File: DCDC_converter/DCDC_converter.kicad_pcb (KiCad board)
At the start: 2 copper layers, 65 x 27 mm, 27 parts, among them J1 Conn_01x02, J2 Conn_01x02, U1 MP2491C

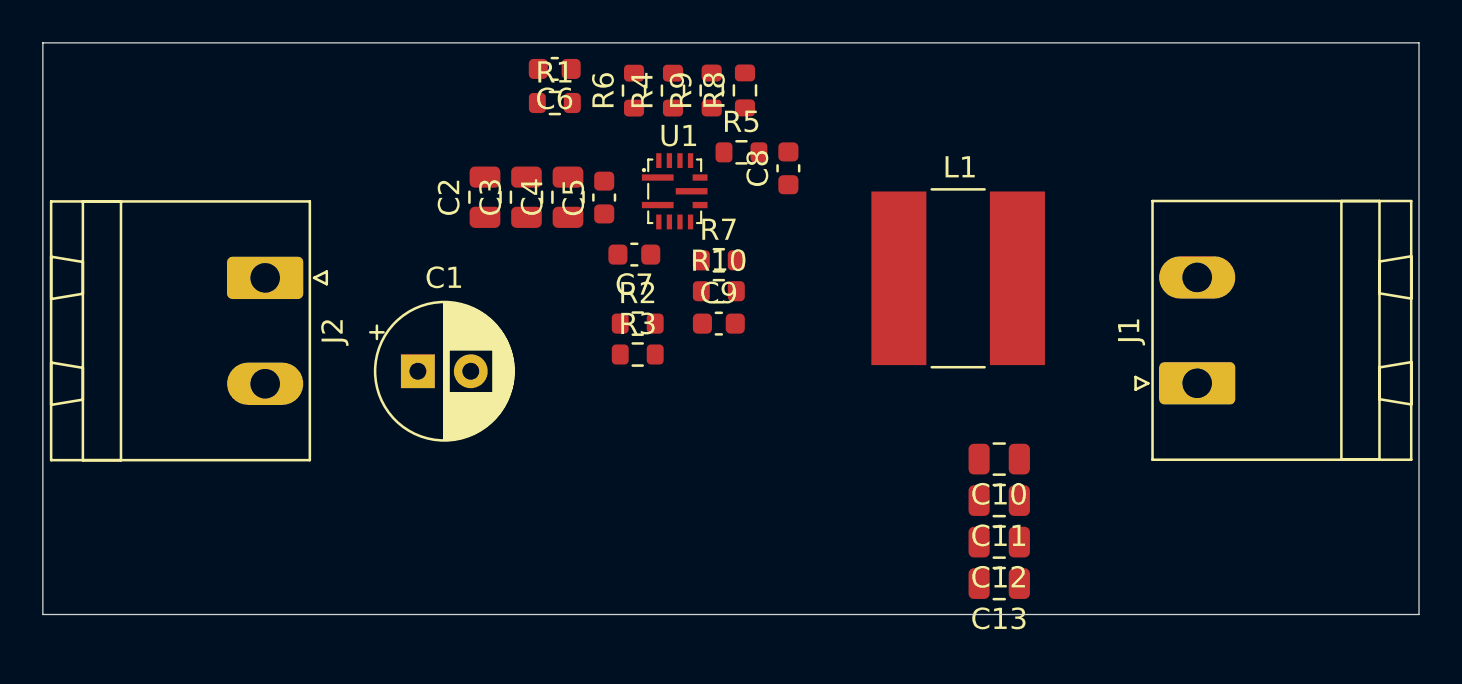
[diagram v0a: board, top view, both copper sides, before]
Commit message: Adjusting elements placement
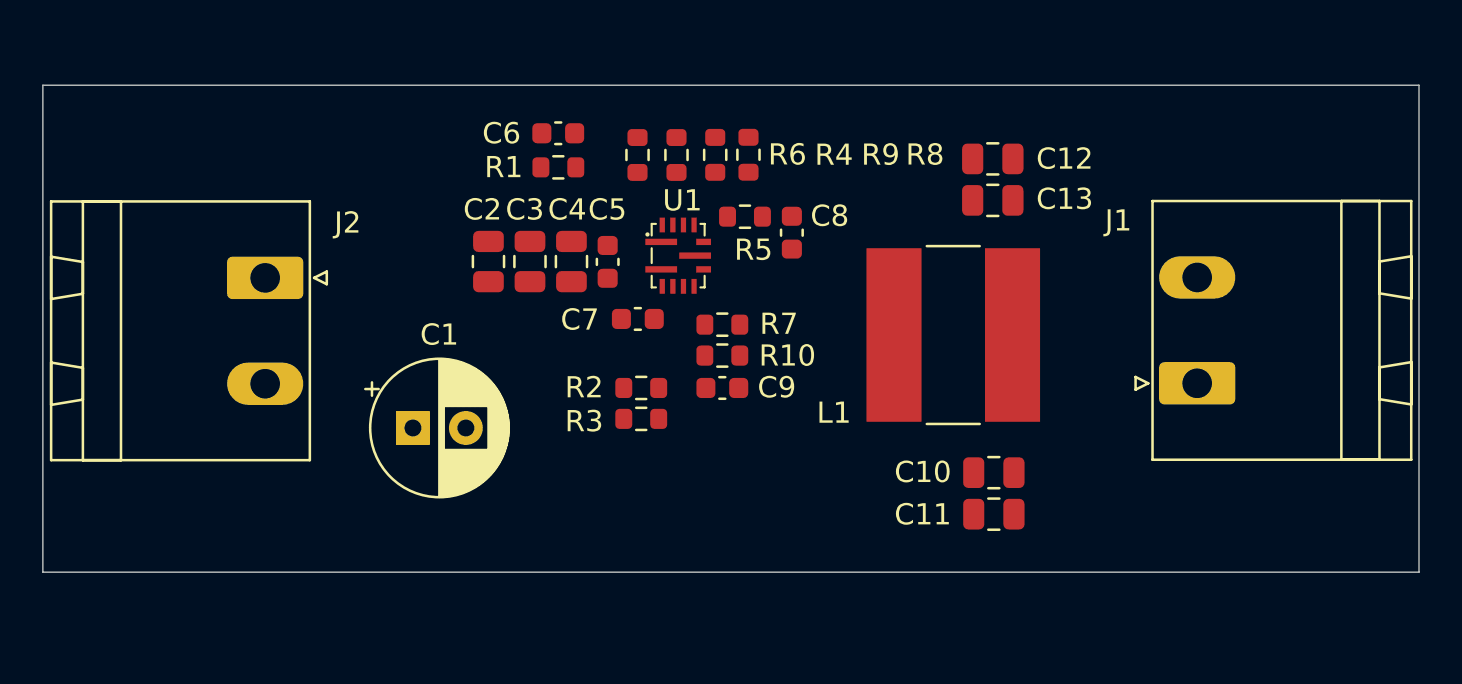
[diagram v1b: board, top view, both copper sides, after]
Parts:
- moved C12 18.1 mm to (204.4, 84.2)
- moved C13 18.1 mm to (204.4, 86.1)
- moved C5 3.04 mm to (186.2, 89.0)
- moved R4 3.04 mm to (189.4, 84.0)
- moved C4 3.04 mm to (184.5, 89.0)
- moved C8 3.04 mm to (194.9, 87.7)
- moved C9 3.04 mm to (191.6, 95.0)
- moved R2 3.04 mm to (187.8, 95.0)
- moved R6 3.04 mm to (187.6, 84.0)
- moved R7 3.04 mm to (191.6, 92.0)
- moved R8 3.04 mm to (192.8, 84.0)
- moved U1 3.04 mm to (189.5, 88.8)
- moved C2 3.04 mm to (180.5, 89.0)
- moved C3 3.04 mm to (182.5, 89.0)
- moved C6 3.04 mm to (183.8, 83.0)
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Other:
- board size 65 x 27 mm -> 65 x 23 mm

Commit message: Changing number of layers of PCB
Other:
- copper layers 2 -> 4
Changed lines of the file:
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@@
 	(layers
 		(0 "F.Cu" signal)
+		(1 "In1.Cu" signal)
+		(2 "In2.Cu" signal)
 		(31 "B.Cu" signal)
 		(32 "B.Adhes" user "B.Adhesive")
@@
 	)
 	(setup
+		(stackup
+			(layer "F.SilkS"
+				(type "Top Silk Screen")
+			)
+			(layer "F.Paste"
+				(type "Top Solder Paste")
+			)
+			(layer "F.Mask"
+				(type "Top Solder Mask")
+				(thickness 0.01)
+			)
+			(layer "F.Cu"
+				(type "copper")
+				(thickness 0.035)
+			)
+			(layer "dielectric 1"
+				(type "prepreg")
+				(thickness 0.1)
+				(material "FR4")
+				(epsilon_r 4.5)
+				(loss_tangent 0.02)
+			)
+			(layer "In1.Cu"
+				(type "copper")
+				(thickness 0.035)
+			)
+			(layer "dielectric 2"
+				(type "core")
+				(thickness 1.24)
+				(material "FR4")
+				(epsilon_r 4.5)
+				(loss_tangent 0.02)
+			)
+			(layer "In2.Cu"
+				(type "copper")
+				(thickness 0.035)
+			)
+			(layer "dielectric 3"
+				(type "prepreg")
+				(thickness 0.1)
+				(material "FR4")
+				(epsilon_r 4.5)
+				(loss_tangent 0.02)
+			)
+			(layer "B.Cu"
+				(type "copper")
+				(thickness 0.035)
+			)
+			(layer "B.Mask"
+				(type "Bottom Solder Mask")
+				(thickness 0.01)
+			)
+			(layer "B.Paste"
+				(type "Bottom Solder Paste")
+			)
+			(layer "B.SilkS"
+				(type "Bottom Silk Screen")
+			)
+			(copper_finish "None")
+			(dielectric_constraints no)
+		)
 		(pad_to_mask_clearance 0)
 		(allow_soldermask_bridges_in_footprints no)

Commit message: Last update
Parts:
- moved R8 2.14 mm to (193.2, 86.1), turned to -90 degrees
- moved R6 2.13 mm to (187.3, 86.1)
- moved R9 2.11 mm to (191.3, 86.1)
- moved C2 2.11 mm to (180.5, 91.1), turned to -90 degrees
- moved C3 2.11 mm to (182.5, 91.1), turned to -90 degrees
- moved C5 2.11 mm to (186.1, 91.2), turned to -90 degrees
- moved C6 2.11 mm to (183.8, 85.1)
- moved C9 2.11 mm to (191.6, 97.1), turned to 180 degrees
- moved R1 2.11 mm to (183.8, 86.7)
- moved R10 2.11 mm to (191.6, 95.6), turned to 180 degrees
- moved R2 2.11 mm to (187.7, 97.1)
- moved R3 2.11 mm to (187.7, 98.6)
- moved R5 2.11 mm to (192.6, 89.0)
- moved U1 2.11 mm to (189.5, 90.9)
- moved C4 2.11 mm to (184.4, 91.1), turned to -90 degrees
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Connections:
- J2 pad 1: GND -> +24V
- J2 pad 2: +24V -> GND
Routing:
- net Net-(U1-SW): track 0.00 -> 10.4 mm
- net VCC: track 0.00 -> 8.21 mm, vias 0 -> 1
- net Net-(U1-EN): track 0.00 -> 7.09 mm, vias 0 -> 2
- net Net-(U1-MODE): track 0.00 -> 5.63 mm
- net Net-(U1-PG): track 0.00 -> 3.17 mm
- net Net-(U1-ILIM): track 0.00 -> 2.55 mm
- net +24V: track 0.00 -> 1.72 mm
- net Net-(U1-BST): track 0.00 -> 1.66 mm
- added copper zone on B.Cu, net +24V
- added copper zone on F.Cu, net +24V
- added copper zone on B.Cu, net +5V
- added copper zone on F.Cu, net +5V

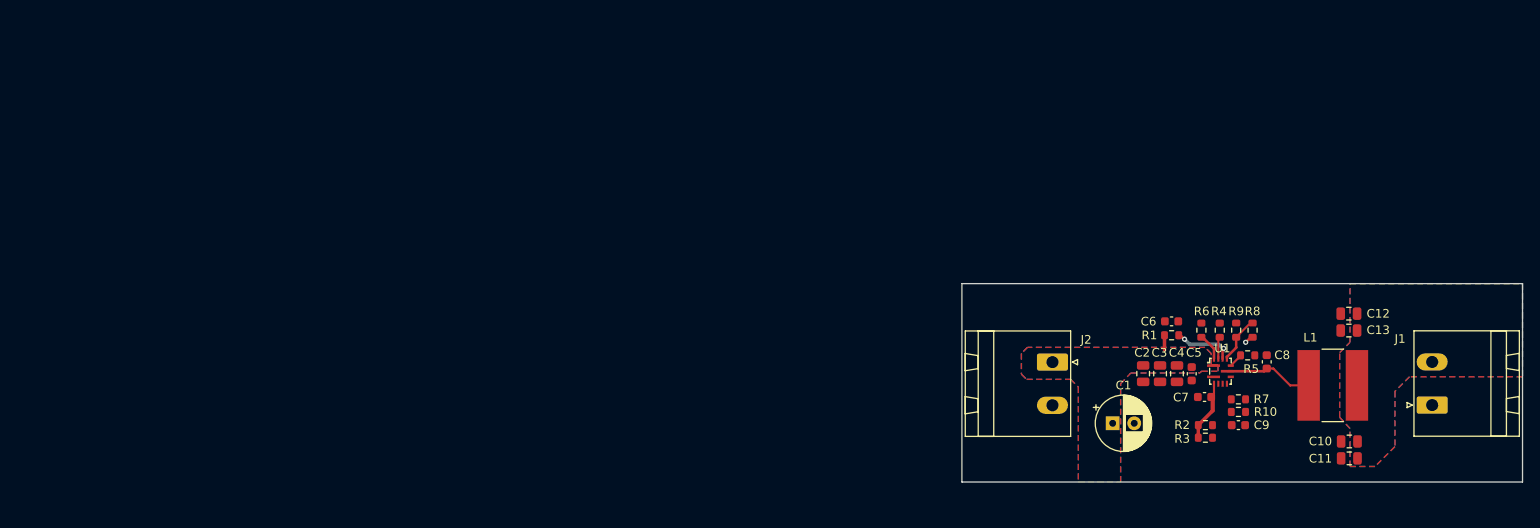
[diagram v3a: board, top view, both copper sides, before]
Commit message: Adjusting the size of the PCB
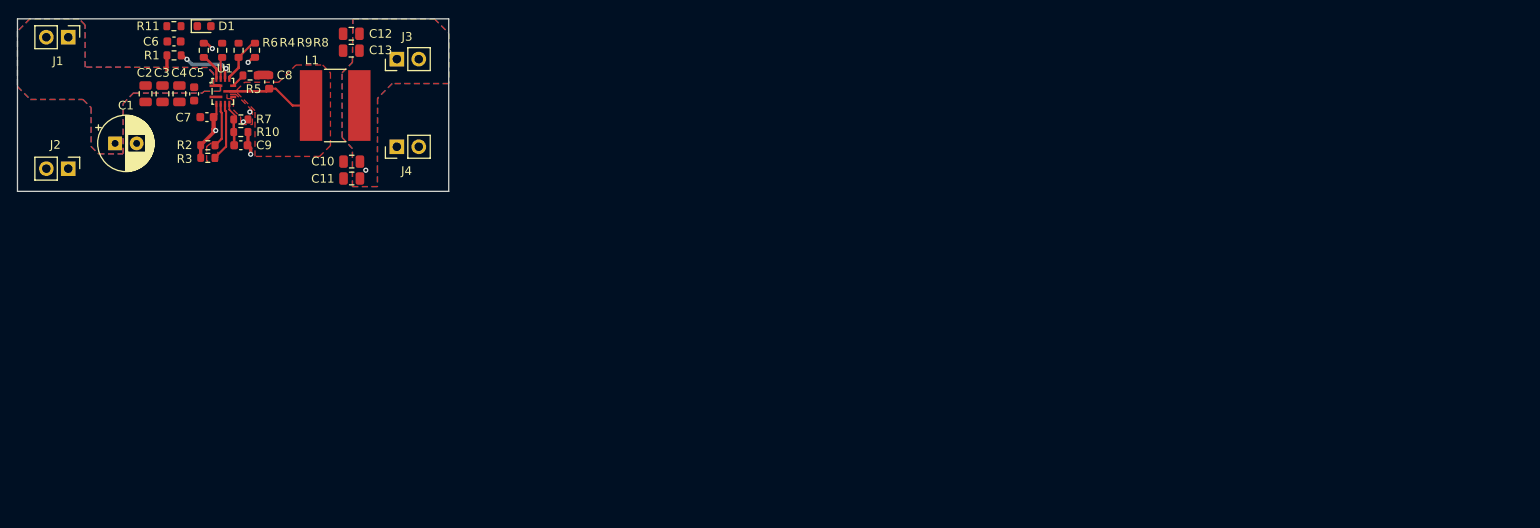
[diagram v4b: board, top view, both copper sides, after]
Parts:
- added D1: LED, LED_SMD:LED_0603_1608Metric, F.Cu at (71.6, 50.9)
- added J3: Conn_01x02_Pin, Connector_PinHeader_2.54mm:PinHeader_1x02_P2.54mm_Vertical, F.Cu at (94.0, 54.7)
- added J4: Conn_01x02_Pin, Connector_PinHeader_2.54mm:PinHeader_1x02_P2.54mm_Vertical, F.Cu at (94.0, 64.8)
- added R11: 1k, Resistor_SMD:R_0603_1608Metric, F.Cu at (68.1, 50.9)
- J1, J2: value Conn_01x02 -> Conn_01x02_Pin; footprint Connector_Phoenix_MSTB:PhoenixContact_MSTBA_2,5_2-G_1x02_P5.00mm_Horizontal -> Connector_PinHeader_2.54mm:PinHeader_1x02_P2.54mm_Vertical
- moved J1 163.8 mm to (55.9, 52.1), turned to -90 degrees
- moved C12 120.1 mm to (88.7, 51.7)
- moved C1 120.1 mm to (61.3, 64.4)
- moved C10 120.1 mm to (88.8, 66.5)
- moved C3 120.1 mm to (66.8, 58.7)
- moved L1 120.1 mm to (86.8, 60.0)
- moved R1 120.1 mm to (68.2, 54.2)
- moved R2 120.1 mm to (72.1, 64.7)
- moved R3 120.1 mm to (72.1, 66.1)
- moved R5 120.1 mm to (77.0, 56.6)
- moved U1 120.1 mm to (73.8, 58.4)
- moved C13 120.1 mm to (88.7, 53.7)
- moved C2 120.1 mm to (64.9, 58.7)
- moved C4 120.1 mm to (68.8, 58.7)
- moved C5 120.1 mm to (70.5, 58.7)
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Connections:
- J1 pad 1: GND -> +24V
- J1 pad 2: +5V -> +24V
- J2 pad 1: +24V -> GND
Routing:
- net +5V: track 0.00 -> 16.9 mm, vias 0 -> 2
- net VCC: track 8.21 -> 24.6 mm, vias 1 -> 3
- net Net-(U1-VSEL2): track 0.00 -> 6.84 mm
- net Net-(U1-FB): track 0.00 -> 5.28 mm
- net Net-(U1-VSEL1): track 0.00 -> 5.16 mm
- net Net-(C8-Pad2): track 0.00 -> 1.22 mm
- net GND: vias 0 -> 2
- added copper zone on F.Cu, net GND
- added copper zone on F.Cu, net Net-(U1-SW)
- added copper zone on F.Cu, net Net-(U1-VSEL1)
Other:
- board size 65 x 23 mm -> 50 x 20 mm

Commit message: Power PCB done
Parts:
- moved C6 0.42 mm to (68.1, 53.0)
- moved D1 0.42 mm to (71.6, 51.3)
- moved R1 0.42 mm to (68.2, 54.7)
- moved R11 0.42 mm to (68.1, 51.3)
- moved C11 0.05 mm to (88.8, 68.5)
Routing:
- net Net-(U1-SW): track 10.4 -> 1.26 mm
- net Net-(D1-K): track 0.00 -> 6.06 mm, vias 0 -> 2
- net Net-(U1-PG): track 3.17 -> 7.52 mm
- net VCC: track 24.6 -> 27.0 mm
- net Net-(U1-EN): track 7.09 -> 8.97 mm
- net +24V: track 1.73 -> 1.30 mm, vias 0 -> 42
- net +5V: track 16.9 -> 17.1 mm, vias 2 -> 13
- net GND: vias 2 -> 72
- added copper zone on B.Cu, net GND
- added copper zone on In1.Cu, net GND
- added copper zone on In2.Cu, net GND

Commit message: Fabricatoin files generated
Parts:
- renumbered J4 to GND, J2 to GND, J1 to IN, J3 to OUT
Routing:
- net +5V: vias 13 -> 10
- net +24V: vias 42 -> 38
